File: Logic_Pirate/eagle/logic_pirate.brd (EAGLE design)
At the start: 30 x 30 mm, 27 parts, among them IC1 TINYLOGIC_PIC32MX250F128BSO, IC2 TINYLOGIC_DP_DEVICES_IC_MEM_2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, IC3 TINYLOGIC_DP_DEVICES_IC_MEM_2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, IC4 TINYLOGIC_DP_DEVICES_IC_74LVC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, J1 DP_DEVICES_CON_HEADER_1X06-SM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, J2 DP_DEVICES_CON_HEADER_1X06-SM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, X1 RESONATORSMD

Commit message: * Increased the offset for the ICSP holes from 2 to 4 mils.
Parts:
- added U$1: (no value), logic_pirate:LP_LOGO
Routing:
- net VCC: track 107.3 -> 108.4 mm, vias 5 -> 6
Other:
- board text removed: "Logic Pirate"
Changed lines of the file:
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@@
 <setting verticaltext="up"/>
 </settings>
-<grid distance="25" unitdist="mil" unit="mil" style="lines" multiple="1" display="yes" altdistance="12.5" altunitdist="mil" altunit="mil"/>
+<grid distance="25" unitdist="mil" unit="mil" style="lines" multiple="1" display="yes" altdistance="6.25" altunitdist="mil" altunit="mil"/>
 <layers>
 <layer number="1" name="Top" color="4" fill="1" visible="yes" active="yes"/>
@@
 <wire x1="17.78" y1="27.6225" x2="17.78" y2="26.9875" width="0.4064" layer="21"/>
 <text x="20.955" y="9.2075" size="1.016" layer="21" ratio="15" rot="R90">ICSP</text>
-<text x="7.62" y="6.0325" size="1.4732" layer="21" ratio="15" rot="R90">Logic Pirate</text>
 <text x="5.3975" y="17.145" size="1.016" layer="22" ratio="15" rot="SMR270">SeeedStudio</text>
 <wire x1="0.635" y1="17.4625" x2="4.1275" y2="17.4625" width="0.1524" layer="22"/>
@@
 <element name="JP4" library="SparkFun" package="FIDUCIAL-1X2" value="FIDUCIAL1X2" x="22.225" y="3.4925" rot="MR0"/>
 <element name="JP5" library="SparkFun" package="FIDUCIAL-1X2" value="FIDUCIAL1X2" x="6.6675" y="23.1775" rot="MR0"/>
+<element name="U$1" library="logic_pirate" package="LP_LOGO" value="" x="6.82625" y="13.335" rot="R90"/>
 </elements>
 <signals>
@@
 <wire x1="5.715" y1="13.6525" x2="5.4275" y2="13.94" width="0.4064" layer="1"/>
 <wire x1="5.4275" y1="13.94" x2="4.58" y2="13.94" width="0.4064" layer="1"/>
-<wire x1="22.5425" y1="11.3792" x2="22.5425" y2="13.0175" width="0.1524" layer="1"/>
+<wire x1="22.5425" y1="11.3284" x2="22.5425" y2="13.0175" width="0.1524" layer="1"/>
 <wire x1="22.5425" y1="13.0175" x2="23.1775" y2="13.6525" width="0.1524" layer="1"/>
 <wire x1="23.1775" y1="13.6525" x2="23.1775" y2="15.875" width="0.1524" layer="1"/>
@@
 <wire x1="21.59" y1="15.875" x2="23.1775" y2="15.875" width="0.1524" layer="1"/>
 <contactref element="C8" pad="2"/>
-<wire x1="22.5425" y1="11.3792" x2="21.6408" y2="10.4775" width="0.1524" layer="1"/>
 <contactref element="IC1" pad="19"/>
 <contactref element="LED1" pad="C"/>
+<wire x1="22.5425" y1="11.3284" x2="21.6916" y2="10.4775" width="0.1524" layer="1"/>
 </signal>
 <signal name="D0">
@@
 <wire x1="17.78" y1="21.59" x2="17.17" y2="20.98" width="0.4064" layer="1"/>
 <wire x1="17.17" y1="20.98" x2="16.27" y2="20.98" width="0.4064" layer="1"/>
-<wire x1="18.67" y1="17.78" x2="19.3675" y2="17.78" width="0.4064" layer="1"/>
-<wire x1="19.3675" y1="17.78" x2="20.32" y2="18.7325" width="0.4064" layer="1"/>
-<wire x1="20.32" y1="19.3675" x2="20.32" y2="18.7325" width="0.4064" layer="1"/>
+<wire x1="18.67" y1="17.78" x2="19.685" y2="17.78" width="0.4064" layer="1"/>
+<wire x1="19.685" y1="17.78" x2="20.32" y2="18.415" width="0.4064" layer="1"/>
+<wire x1="20.32" y1="19.685" x2="20.32" y2="18.415" width="0.4064" layer="1"/>
 <wire x1="9.27" y1="2.54" x2="13.335" y2="2.54" width="0.4064" layer="1"/>
 <wire x1="13.335" y1="2.54" x2="13.335" y2="3.81" width="0.4064" layer="1"/>
@@
 <contactref element="JP1" pad="2"/>
 <wire x1="11.1125" y1="25.7175" x2="10.375" y2="26.455" width="0.4064" layer="1"/>
-<wire x1="21.5392" y1="9.2075" x2="20.955" y2="9.2075" width="0.1524" layer="1"/>
-<wire x1="20.955" y1="9.2075" x2="20.6375" y2="8.89" width="0.1524" layer="1"/>
-<wire x1="20.6375" y1="8.89" x2="20.6375" y2="3.4925" width="0.1524" layer="1"/>
+<wire x1="20.6375" y1="8.3566" x2="20.6375" y2="3.4925" width="0.1524" layer="1"/>
 <contactref element="C8" pad="1"/>
 <wire x1="18.415" y1="20" x2="18.415" y2="19.685" width="0.4064" layer="16"/>
 <wire x1="18.835" y1="22.645" x2="18.835" y2="21.59" width="0.4064" layer="1"/>
-<wire x1="20.32" y1="19.3675" x2="18.835" y2="20.8525" width="0.4064" layer="1"/>
-<wire x1="18.835" y1="20.8525" x2="18.835" y2="21.59" width="0.4064" layer="1"/>
+<wire x1="20.32" y1="19.685" x2="19.685" y2="20.32" width="0.4064" layer="1"/>
+<wire x1="19.685" y1="20.32" x2="19.20875" y2="20.32" width="0.4064" layer="1"/>
+<wire x1="19.20875" y1="20.32" x2="18.835" y2="20.69375" width="0.4064" layer="1"/>
+<wire x1="18.835" y1="20.69375" x2="18.835" y2="21.59" width="0.4064" layer="1"/>
 <wire x1="18.415" y1="20" x2="18.515" y2="19.9" width="0.4064" layer="16"/>
 <wire x1="18.515" y1="19.9" x2="20.6375" y2="19.9" width="0.4064" layer="16"/>
@@
 <wire x1="20.6375" y1="3.4925" x2="21.4875" y2="3.4925" width="0.1524" layer="1"/>
 <wire x1="21.4875" y1="3.4925" x2="21.59" y2="3.595" width="0.1524" layer="1"/>
+<via x="21.2725" y="22.86" extent="1-16" drill="0.3302"/>
+<wire x1="22.225" y1="22.86" x2="21.2725" y2="22.86" width="0.4064" layer="16"/>
+<wire x1="20.6375" y1="8.3566" x2="21.4884" y2="9.2075" width="0.1524" layer="1"/>
 </signal>
 <signal name="VBUS">
@@
 <wire x1="18.67" y1="2.54" x2="22.225" y2="2.54" width="0.1524" layer="1"/>
 <wire x1="22.225" y1="2.54" x2="22.5425" y2="2.8575" width="0.1524" layer="1"/>
-<wire x1="21.59" y1="5.295" x2="21.59" y2="7.8867" width="0.1524" layer="1"/>
-<wire x1="21.59" y1="7.8867" x2="21.6408" y2="7.9375" width="0.1524" layer="1"/>
+<wire x1="21.59" y1="5.295" x2="21.59" y2="7.8359" width="0.1524" layer="1"/>
 <wire x1="22.5425" y1="2.8575" x2="22.5425" y2="5.08" width="0.1524" layer="1"/>
 <wire x1="22.5425" y1="5.08" x2="22.3275" y2="5.295" width="0.1524" layer="1"/>
 <wire x1="22.3275" y1="5.295" x2="21.59" y2="5.295" width="0.1524" layer="1"/>
+<wire x1="21.59" y1="7.8359" x2="21.6916" y2="7.9375" width="0.1524" layer="1"/>
 </signal>
 <signal name="PGED">
 <contactref element="JP1" pad="4"/>
 <contactref element="IC1" pad="2"/>
-<wire x1="20.32" y1="10.5283" x2="20.32" y2="4.445" width="0.1524" layer="1"/>
+<wire x1="20.32" y1="10.5791" x2="20.32" y2="4.445" width="0.1524" layer="1"/>
 <wire x1="20.32" y1="4.445" x2="19.685" y2="3.81" width="0.1524" layer="1"/>
 <wire x1="19.685" y1="3.81" x2="18.67" y2="3.81" width="0.1524" layer="1"/>
-<wire x1="20.32" y1="10.5283" x2="21.5392" y2="11.7475" width="0.1524" layer="1"/>
+<wire x1="20.32" y1="10.5791" x2="21.4884" y2="11.7475" width="0.1524" layer="1"/>
 </signal>
 <signal name="PGEC">
 <contactref element="JP1" pad="5"/>
 <contactref element="IC1" pad="3"/>
-<wire x1="20.0025" y1="11.3792" x2="20.0025" y2="5.3975" width="0.1524" layer="1"/>
+<wire x1="20.0025" y1="12.065" x2="20.0025" y2="5.3975" width="0.1524" layer="1"/>
 <wire x1="20.0025" y1="5.3975" x2="19.685" y2="5.08" width="0.1524" layer="1"/>
 <wire x1="19.685" y1="5.08" x2="18.67" y2="5.08" width="0.1524" layer="1"/>
-<wire x1="20.0025" y1="11.3792" x2="21.6408" y2="13.0175" width="0.1524" layer="1"/>
+<wire x1="20.0025" y1="12.065" x2="20.955" y2="13.0175" width="0.1524" layer="1"/>
+<wire x1="20.955" y1="13.0175" x2="21.6916" y2="13.0175" width="0.1524" layer="1"/>
 </signal>
 <signal name="D-">

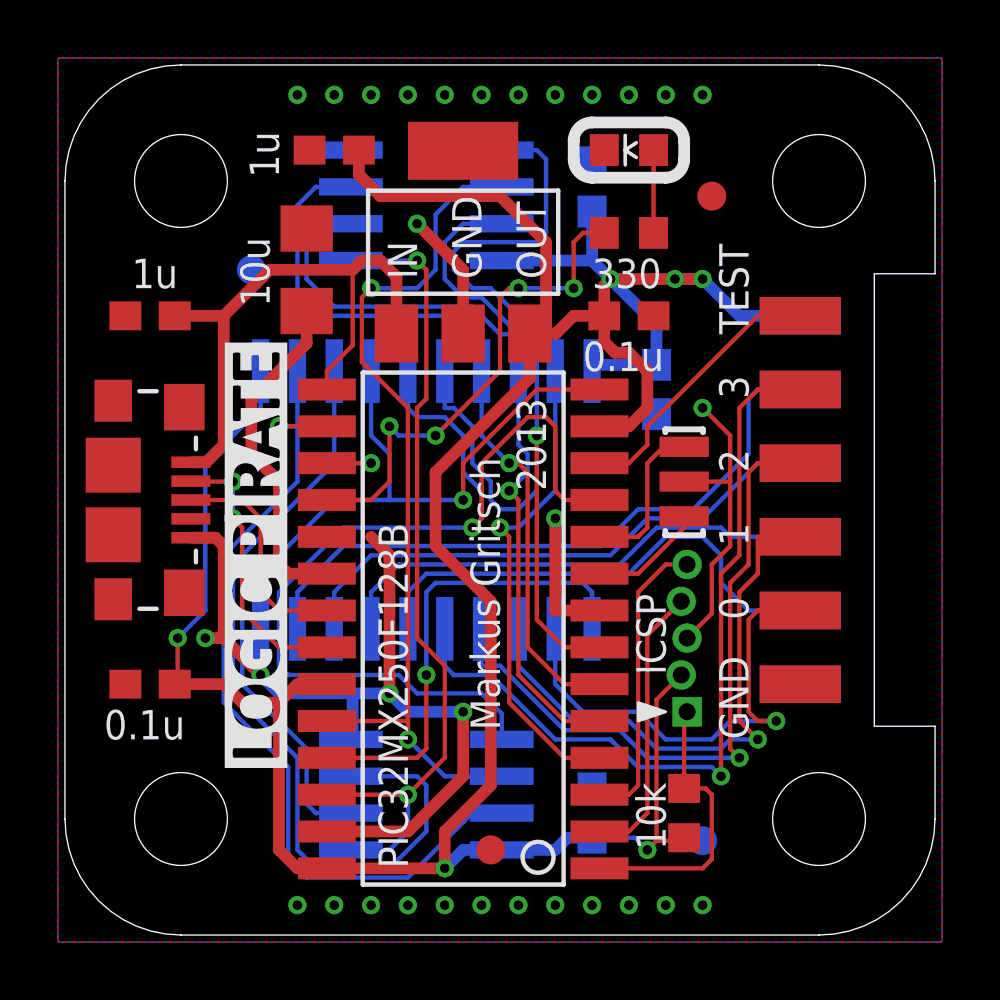
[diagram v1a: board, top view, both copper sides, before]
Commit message: 
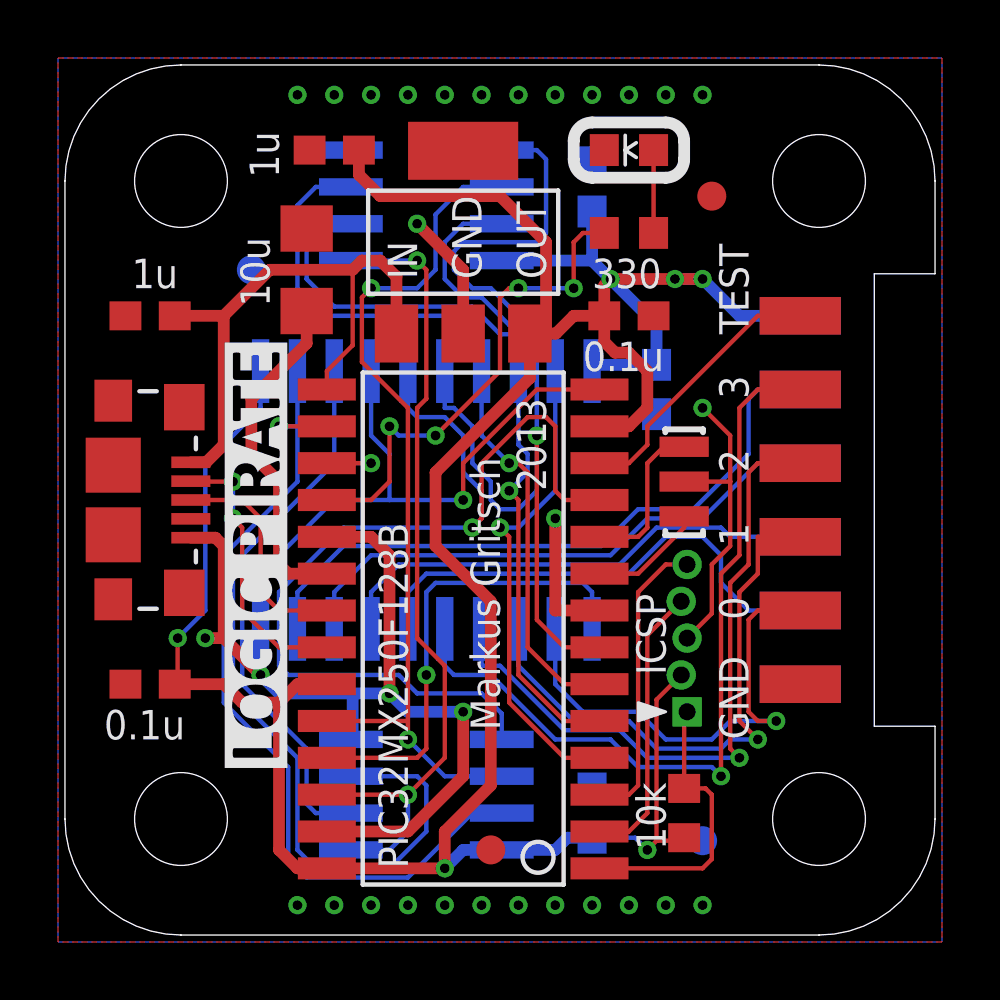
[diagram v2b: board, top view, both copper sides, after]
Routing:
- net GND: track 51.5 -> 53.0 mm
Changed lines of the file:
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@@
 <via x="6.985" y="9.2075" extent="1-16" drill="0.3302"/>
 <wire x1="6.985" y1="9.2075" x2="5.715" y2="10.4775" width="0.4064" layer="1"/>
-<wire x1="10.795" y1="13.97" x2="11.43" y2="13.335" width="0.4064" layer="1"/>
 <wire x1="11.43" y1="13.335" x2="11.43" y2="8.5725" width="0.4064" layer="1"/>
 <via x="11.43" y="8.5725" extent="1-16" drill="0.3302"/>
@@
 <contactref element="LED1" pad="C"/>
 <wire x1="22.5425" y1="11.3284" x2="21.6916" y2="10.4775" width="0.1524" layer="1"/>
+<wire x1="11.43" y1="13.335" x2="10.795" y2="13.97" width="0.4064" layer="1"/>
+<wire x1="10.795" y1="13.97" x2="9.27" y2="13.97" width="0.4064" layer="1"/>
 </signal>
 <signal name="D0">
